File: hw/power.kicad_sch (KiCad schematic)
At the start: 56 parts, among them J9 Expansion, U1 RT8096B, U2 RT8096B, U25 TLV75801PDBV, U3 RT8096B, U5 TPS563249DDC

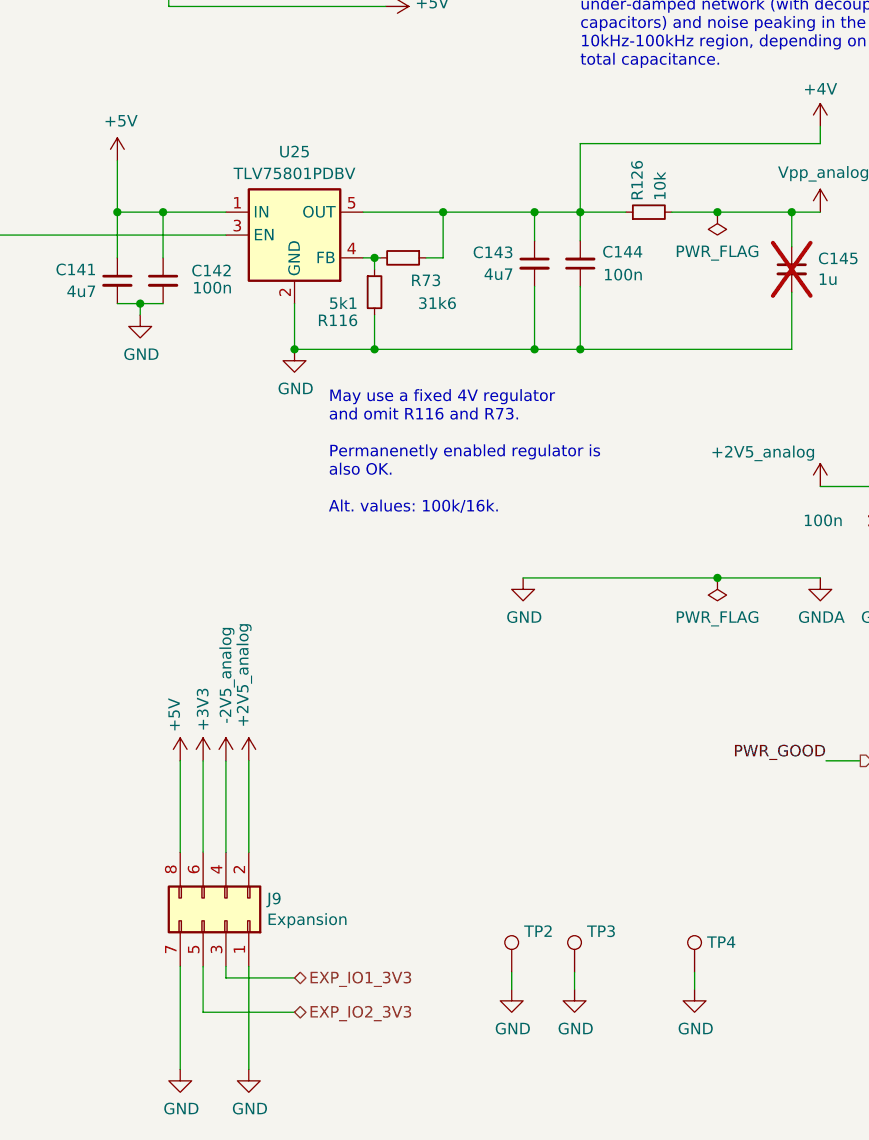
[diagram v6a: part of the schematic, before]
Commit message: updated parts assignments
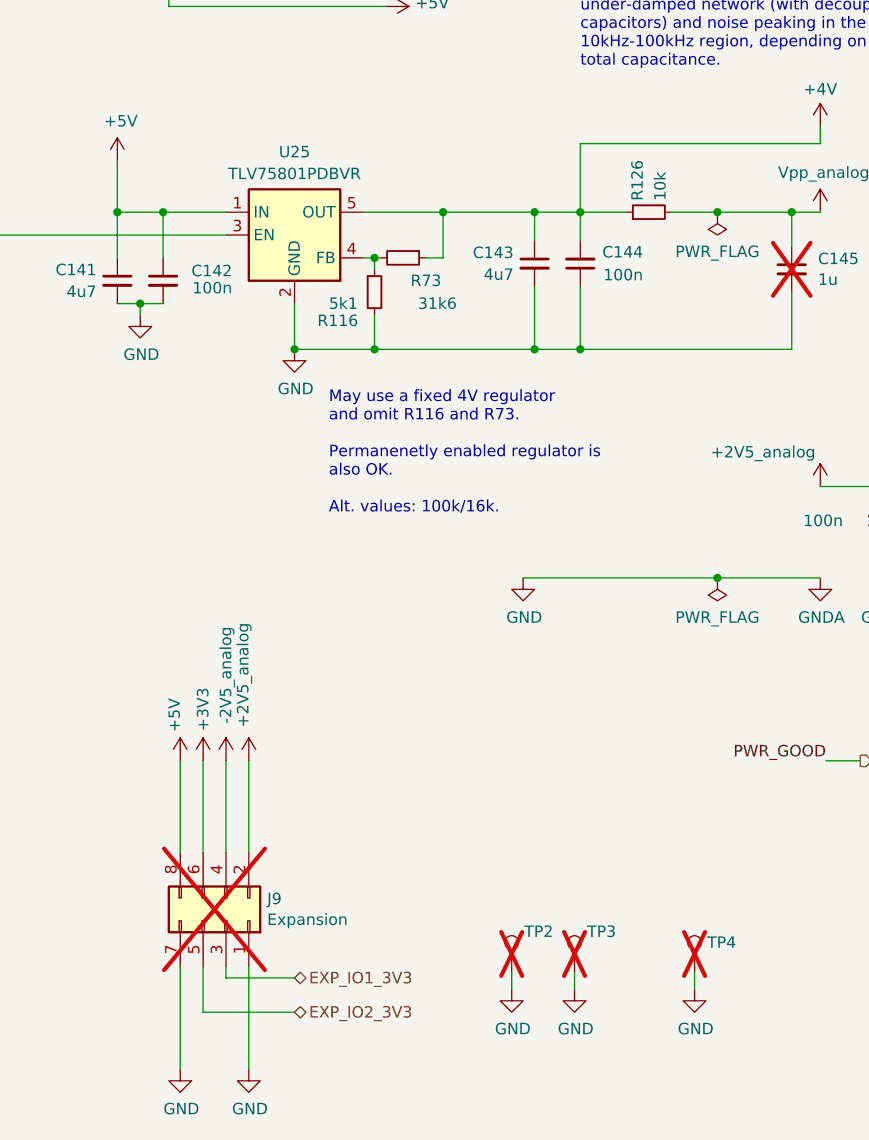
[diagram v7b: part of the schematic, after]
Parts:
- C14, C4: Manufacturer (none) -> Walsin; Part (none) -> 0603N470J101CT
- J9: now not fitted
- L1, L2, L3, L4: Manufacturer (none) -> Pulse; Part (none) -> BDCD002520121R5MS1
- R1, R15, R5: Manufacturer (none) -> Stackpole; Part (none) -> RMCF0603FT100K
- R10, R126, R2, R3, R4, R8: Manufacturer (none) -> Stackpole; Part (none) -> RMCF0603FT10K0
- R116: Manufacturer (none) -> Stackpole; Part (none) -> RMCF0603FT5K10
- R6: Manufacturer (none) -> Stackpole; Part (none) -> RMCF0603FT45K3
- R69, R72: Manufacturer (none) -> Stackpole; Part (none) -> RMCF0603ZT0R00
- R7, R73, R9: Manufacturer (none) -> Stackpole; Part (none) -> RMCF0603FT31K6
- TP2, TP3, TP4: now not fitted; now left out of the parts list
- U1, U2, U3: Part RT8096B -> RT8096BHGE
- U25: value TLV75801PDBV -> TLV75801PDBVR; Manufacturer (none) -> TI; Part (none) -> TLV75801PDBVR
- U5: Manufacturer (none) -> TI; Part (none) -> TPS563249DDCR
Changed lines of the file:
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@@
 			)
 		)
-		(property "Part" "RT8096B"
+		(property "Part" "RT8096BHGE"
 			(at 69.85 72.39 0)
 			(effects
@@
 			)
 		)
-		(property "Part" ""
+		(property "Part" "BDCD002520121R5MS1"
 			(at 85.09 69.85 90)
 			(effects
@@
 			)
 		)
-		(property "Manufacturer" ""
+		(property "Manufacturer" "Pulse"
 			(at 85.09 69.85 90)
 			(effects
@@
 			)
 		)
-		(property "Part" ""
+		(property "Part" "RMCF0603FT10K0"
 			(at 81.28 77.47 0)
 			(effects
@@
 			)
 		)
-		(property "Manufacturer" ""
+		(property "Manufacturer" "Stackpole"
 			(at 81.28 77.47 0)
 			(effects
@@
 			)
 		)
-		(property "Part" ""
+		(property "Part" "RMCF0603FT45K3"
 			(at 90.17 72.39 90)
 			(effects
@@
 			)
 		)
-		(property "Manufacturer" ""
+		(property "Manufacturer" "Stackpole"
 			(at 90.17 72.39 90)
 			(effects
@@
 			)
 		)
-		(property "Part" ""
+		(property "Part" "0603N470J101CT"
 			(at 90.17 76.2 90)
 			(effects
@@
 			)
 		)
-		(property "Manufacturer" ""
+		(property "Manufacturer" "Walsin"
 			(at 90.17 76.2 90)
 			(effects
@@
 			)
 		)
-		(property "Part" "RT8096B"
+		(property "Part" "RT8096BHGE"
 			(at 69.85 109.22 0)
 			(effects
@@
 			)
 		)
-		(property "Part" ""
+		(property "Part" "RMCF0603FT31K6"
 			(at 90.17 109.22 90)
 			(effects
@@
 			)
 		)
-		(property "Manufacturer" ""
+		(property "Manufacturer" "Stackpole"
 			(at 90.17 109.22 90)
 			(effects
@@
 			)
 		)
-		(property "Part" "RT8096B"
+		(property "Part" "RT8096BHGE"
 			(at 69.85 34.29 0)
 			(effects
@@
 			)
 		)
-		(property "Part" ""
+		(property "Part" "BDCD002520121R5MS1"
 			(at 85.09 31.75 90)
 			(effects
@@
 			)
 		)
-		(property "Manufacturer" ""
+		(property "Manufacturer" "Pulse"
 			(at 85.09 31.75 90)
 			(effects
@@
 			)
 		)
-		(property "Part" ""
+		(property "Part" "RMCF0603FT10K0"
 			(at 81.28 114.3 0)
 			(effects
@@
 			)
 		)
-		(property "Manufacturer" ""
+		(property "Manufacturer" "Stackpole"
 			(at 81.28 114.3 0)
 			(effects
@@
 			)
 		)
-		(property "Part" ""
+		(property "Part" "RMCF0603FT10K0"
 			(at 81.28 39.37 0)
 			(effects
@@
 			)
 		)
-		(property "Manufacturer" ""
+		(property "Manufacturer" "Stackpole"
 			(at 81.28 39.37 0)
 			(effects
@@
 			)
 		)
-		(property "Part" ""
+		(property "Part" "RMCF0603FT10K0"
 			(at 90.17 34.29 0)
 			(effects
@@
 			)
 		)
-		(property "Manufacturer" ""
+		(property "Manufacturer" "Stackpole"
 			(at 90.17 34.29 0)
 			(effects
@@
 			)
 		)
-		(property "Part" ""
+		(property "Part" "RMCF0603FT100K"
 			(at 58.42 87.63 0)
 			(effects
@@
 			)
 		)
-		(property "Manufacturer" ""
+		(property "Manufacturer" "Stackpole"
 			(at 58.42 87.63 0)
 			(effects
@@
 			)
 		)
-		(property "Part" ""
+		(property "Part" "RMCF0603FT100K"
 			(at 58.42 50.8 0)
 			(effects
@@
 			)
 		)
-		(property "Manufacturer" ""
+		(property "Manufacturer" "Stackpole"
 			(at 58.42 50.8 0)
 			(effects
@@
 		(in_bom yes)
 		(on_board yes)
-		(dnp no)
+		(dnp yes)
 		(property "Reference" "J9"
 			(at 191.262 134.7216 90)
@@
 			)
 		)
+		(property "Manufacturer" "Stackpole"
+			(at 233.68 58.42 0)
+			(effects
+				(font
+					(size 1.27 1.27)
+				)
+				(hide yes)
+			)
+		)
+		(property "Part" "RMCF0603FT10K0"
+			(at 233.68 58.42 0)
+			(effects
+				(font
+					(size 1.27 1.27)
+				)
+				(hide yes)
+			)
+		)
 		(pin "1"
 		)
@@
 			)
 		)
+		(property "Manufacturer" "TI"
+			(at 88.9 140.97 0)
+			(effects
+				(font
+					(size 1.27 1.27)
+				)
+				(hide yes)
+			)
+		)
+		(property "Part" "TPS563249DDCR"
+			(at 88.9 140.97 0)
+			(effects
+				(font
+					(size 1.27 1.27)
+				)
+				(hide yes)
+			)
+		)
 		(pin "1"
 		)
@@
 			)
 		)
-		(property "Part" ""
+		(property "Part" "  RMCF0603ZT0R00"
 			(at 116.84 31.75 0)
 			(effects
@@
 			)
 		)
-		(property "Manufacturer" ""
+		(property "Manufacturer" "Stackpole"
 			(at 116.84 31.75 0)
 			(effects
@@
 			)
 		)
+		(property "Manufacturer" "Stackpole"
+			(at 203.2 67.31 0)
+			(effects
+				(font
+					(size 1.27 1.27)
+				)
+				(hide yes)
+			)
+		)
+		(property "Part" "RMCF0603FT5K10"
+			(at 203.2 67.31 0)
+			(effects
+				(font
+					(size 1.27 1.27)
+				)
+				(hide yes)
+			)
+		)
 		(pin "1"
 		)
@@
 		(unit 1)
 		(exclude_from_sim no)
-		(in_bom yes)
+		(in_bom no)
 		(on_board yes)
-		(dnp no)
+		(dnp yes)
 		(fields_autoplaced yes)
 		(property "Reference" "TP2"
@@
 			)
 		)
+		(property "Manufacturer" "Walsin"
+			(at 115.57 142.24 0)
+			(effects
+				(font
+					(size 1.27 1.27)
+				)
+				(hide yes)
+			)
+		)
+		(property "Part" "0603N470J101CT"
+			(at 115.57 142.24 0)
+			(effects
+				(font
+					(size 1.27 1.27)
+				)
+				(hide yes)
+			)
+		)
 		(pin "1"
 		)
@@
 			)
 		)
-		(property "Part" ""
+		(property "Part" "BDCD002520121R5MS1"
 			(at 110.49 138.43 90)
 			(effects
@@
 			)
 		)
-		(property "Manufacturer" ""
+		(property "Manufacturer" "Pulse"
 			(at 110.49 138.43 90)
 			(effects
@@
 			)
 		)
-		(property "Value" "TLV75801PDBV"
+		(property "Value" "TLV75801PDBVR"
 			(at 194.31 54.1599 0)
 			(effects
@@
 			)
 		)
+		(property "Manufacturer" "TI"
+			(at 194.31 60.96 0)
+			(effects
+				(font
+					(size 1.27 1.27)
+				)
+				(hide yes)
+			)
+		)
+		(property "Part" "TLV75801PDBVR"
+			(at 194.31 60.96 0)
+			(effects
+				(font
+					(size 1.27 1.27)
+				)
+				(hide yes)
+			)
+		)
 		(pin "3"
 		)
@@
 		(unit 1)
 		(exclude_from_sim no)
-		(in_bom yes)
+		(in_bom no)
 		(on_board yes)
-		(dnp no)
+		(dnp yes)
 		(fields_autoplaced yes)
 		(property "Reference" "TP4"
@@
 			)
 		)
-		(property "Part" ""
+		(property "Part" "  RMCF0603ZT0R00"
 			(at 115.57 69.85 0)
 			(effects
@@
 			)
 		)
-		(property "Manufacturer" ""
+		(property "Manufacturer" "Stackpole"
 			(at 115.57 69.85 0)
 			(effects
@@
 		(unit 1)
 		(exclude_from_sim no)
-		(in_bom yes)
+		(in_bom no)
 		(on_board yes)
-		(dnp no)
+		(dnp yes)
 		(fields_autoplaced yes)
 		(property "Reference" "TP3"
@@
 			)
 		)
-		(property "Part" ""
+		(property "Part" "BDCD002520121R5MS1"
 			(at 85.09 106.68 90)
 			(effects
@@
 			)
 		)
-		(property "Manufacturer" ""
+		(property "Manufacturer" "Pulse"
 			(at 85.09 106.68 90)
 			(effects
@@
 			)
 		)
-		(property "Part" ""
+		(property "Part" "RMCF0603FT100K"
 			(at 158.75 56.515 0)
 			(effects
@@
 			)
 		)
-		(property "Manufacturer" ""
+		(property "Manufacturer" "Stackpole"
 			(at 158.75 56.515 0)
 			(effects
@@
 			)
 		)
+		(property "Manufacturer" "Stackpole"
+			(at 119.38 149.86 0)
+			(effects
+				(font
+					(size 1.27 1.27)
+				)
+				(hide yes)
+			)
+		)
+		(property "Part" "RMCF0603FT10K0"
+			(at 119.38 149.86 0)
+			(effects
+				(font
+					(size 1.27 1.27)
+				)
+				(hide yes)
+			)
+		)
 		(pin "1"
 		)
@@
 			)
 		)
-		(property "Part" ""
+		(property "Part" "RMCF0603FT31K6"
 			(at 206.375 63.5 90)
 			(effects
@@
 			)
 		)
-		(property "Manufacturer" ""
+		(property "Manufacturer" "Stackpole"
 			(at 206.375 63.5 90)
 			(effects
@@
 			(at 119.38 142.24 0)
 			(effects
+				(font
+					(size 1.27 1.27)
+				)
+				(hide yes)
+			)
+		)
+		(property "Manufacturer" "Stackpole"
+			(at 119.38 142.24 0)
+			(effects
+				(font
+					(size 1.27 1.27)
+				)
+				(hide yes)
+			)
+		)
+		(property "Part" "RMCF0603FT31K6"
+			(at 119.38 142.24 0)
+			(effects

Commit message: connected versaclock CLKSEL to ULPI RSTB (share FPGA pin)
ULPI Rstb is unlikely to be used

Also: - update of kicad to 9.0 (many library footprints updated)
      - added sheet titles, author
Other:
- company: (none) -> Till Straumann
- title: (none) -> Power Supply and Expansion Connector
